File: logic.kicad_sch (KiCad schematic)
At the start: 25 parts, among them J101 PogoPin, J102 PogoPin, Q101 NMOS, U101 ATtiny404-SS

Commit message: led
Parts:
- removed D102, D104, D107, D108: LED, LED_SMD:LED_PLCC_2835_Handsoldering, symbol Device:LED
- removed R104, R107, R108: 47Ω, Resistor_SMD:R_1206_3216Metric_Pad1.30x1.75mm_HandSolder, symbol Device:R
- added D101: LED, LED_SMD:LED_PLCC_2835_Handsoldering, symbol Device:LED
- added J101: PogoPin, LIB:0906015207614110, symbol Connector:Conn_01x01_Pin
- added Q101: NMOS, Package_TO_SOT_SMD:SOT-23-3, symbol Simulation_SPICE:NMOS
- added R101: 47Ω, Resistor_SMD:R_1206_3216Metric_Pad1.30x1.75mm_HandSolder, symbol Device:R
- added R103: 100Ω, Resistor_SMD:R_1206_3216Metric_Pad1.30x1.75mm_HandSolder, symbol Device:R
- R102: value 47Ω -> 10kΩ; manf# ERJ-P08J470V -> ERJ-8GEYJ103V
- renumbered D101 to D102, D106 to D104, D109 to D105, D110 to D106, D105 to D107, J101 to J102, J102 to J103, Q101 to Q102, R101 to R104, R106 to R105, R109 to R106, R103 to R107, R105 to R108, R110 to R109, R111 to R110
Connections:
- net +5V: now also R101.2; no longer R102.2
- net GND: now also R102.2, Q101.3 (S)
- net at R102.1: now also Q101.2 (G), R103.1
- new net: D101.2 (A), R101.1
- new net: D101.1 (K), Q101.1 (D)
- new net *_LED: R103.2
- new net *_S: J101.1 (Pin_1)

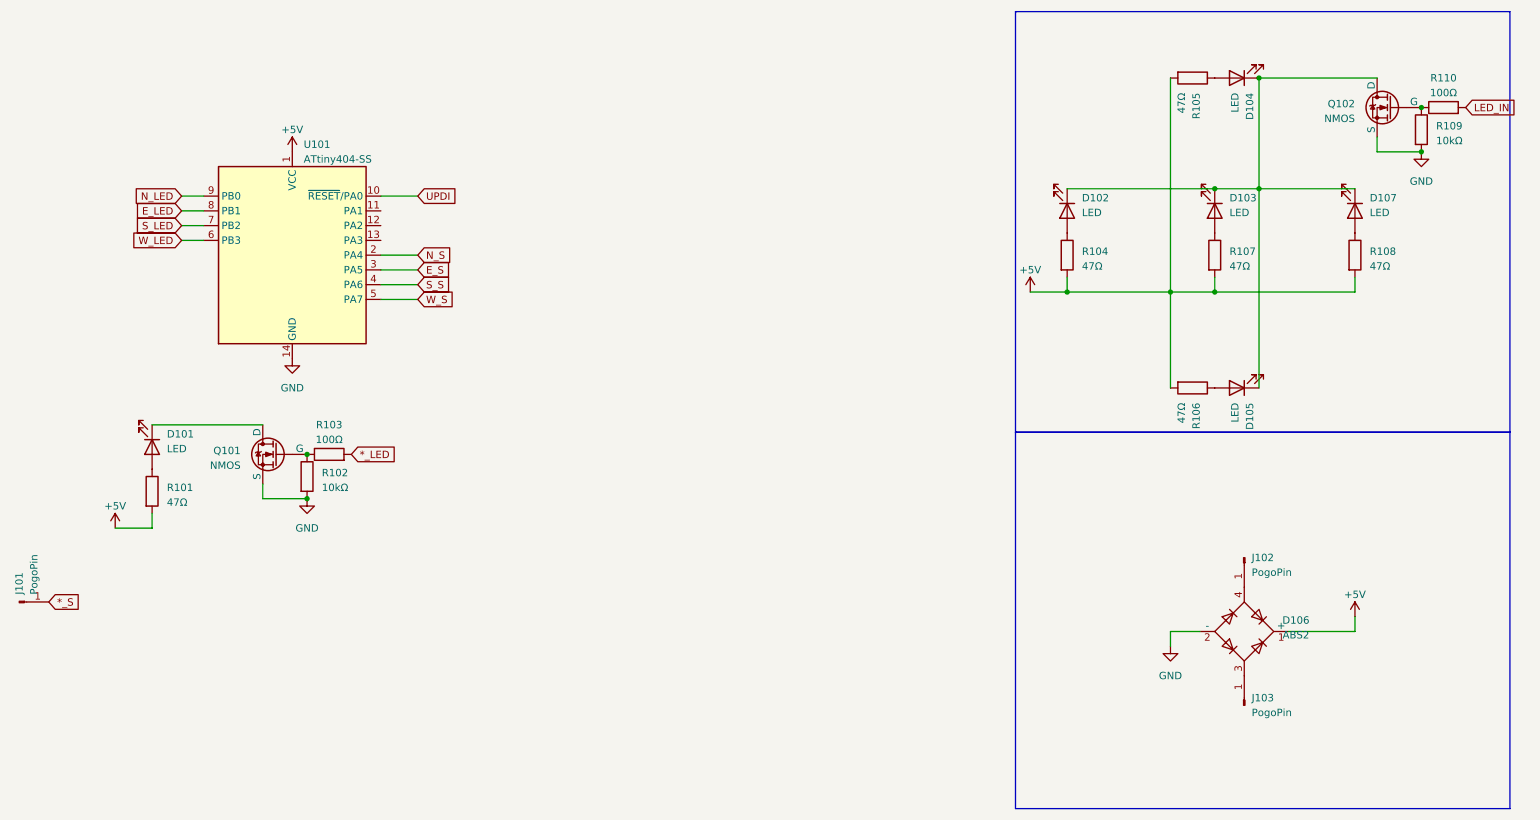
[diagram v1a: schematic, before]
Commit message: block&led
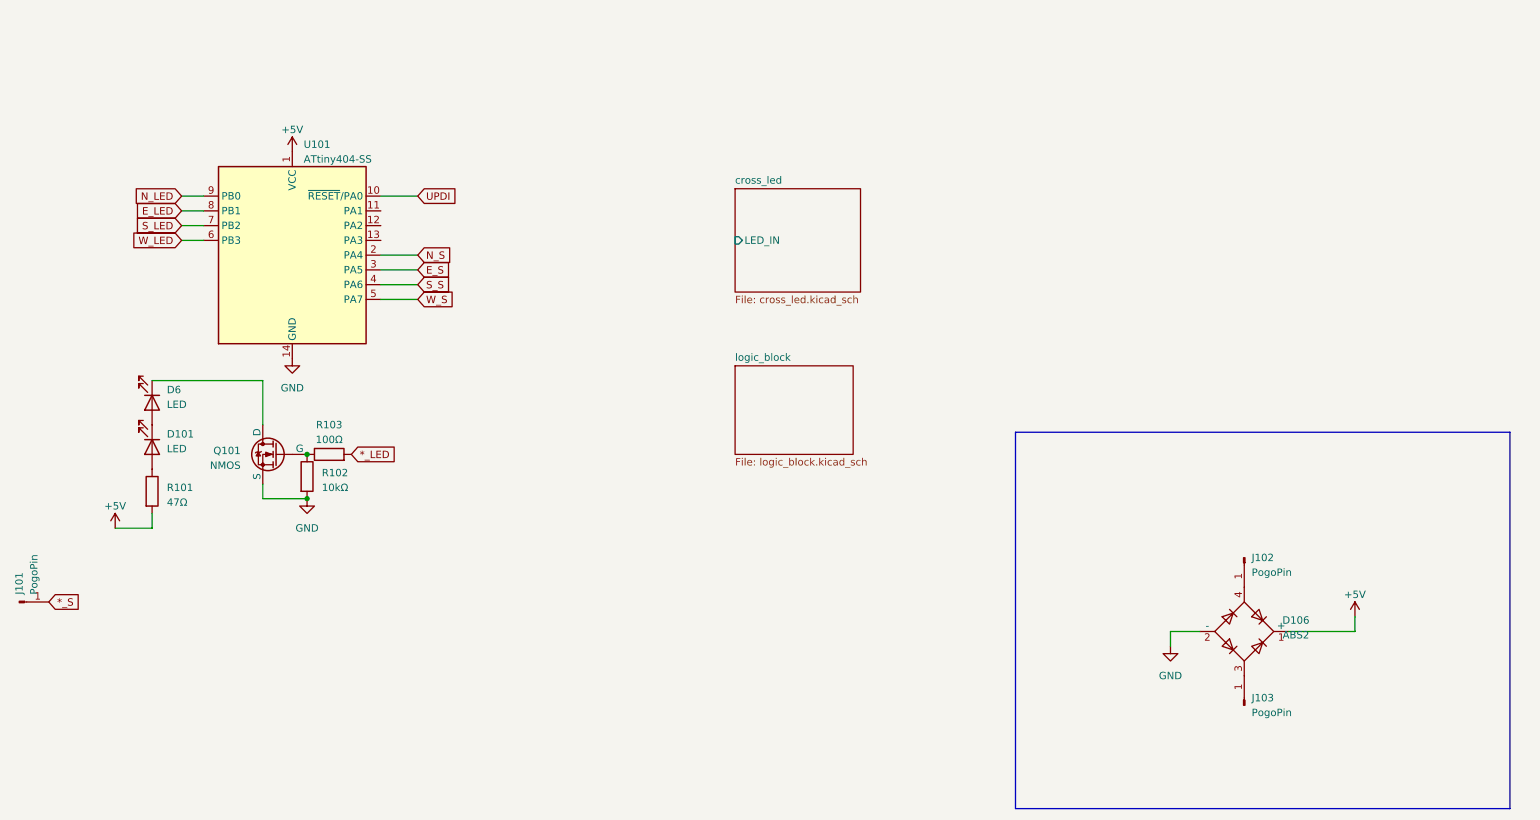
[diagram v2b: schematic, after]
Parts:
- removed D102, D103, D104, D105, D107: LED, LED_SMD:LED_PLCC_2835_Handsoldering, symbol Device:LED
- removed Q102: NMOS, Package_TO_SOT_SMD:SOT-23-3, symbol Simulation_SPICE:NMOS
- removed R104, R105, R106, R107, R108: 47Ω, Resistor_SMD:R_1206_3216Metric_Pad1.30x1.75mm_HandSolder, symbol Device:R
- removed R109: 10kΩ, Resistor_SMD:R_1206_3216Metric_Pad1.30x1.75mm_HandSolder, symbol Device:R
- removed R110: 100Ω, Resistor_SMD:R_1206_3216Metric_Pad1.30x1.75mm_HandSolder, symbol Device:R
- added D6: LED, LED_SMD:LED_PLCC_2835_Handsoldering, symbol Device:LED
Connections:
- net at D101.1 (K): now also D6.2 (A); no longer Q101.1 (D)
- new net: D6.1 (K), Q101.1 (D)
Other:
- added sheet cross_led (cross_led.kicad_sch)
- added sheet logic_block (logic_block.kicad_sch)

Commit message: all
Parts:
- removed D101, D6: LED, LED_SMD:LED_PLCC_2835_Handsoldering, symbol Device:LED
- removed J101: PogoPin, LIB:0906015207614110, symbol Connector:Conn_01x01_Pin
- removed Q101: NMOS, Package_TO_SOT_SMD:SOT-23-3, symbol Simulation_SPICE:NMOS
- removed R101: 47Ω, Resistor_SMD:R_1206_3216Metric_Pad1.30x1.75mm_HandSolder, symbol Device:R
- removed R102: 10kΩ, Resistor_SMD:R_1206_3216Metric_Pad1.30x1.75mm_HandSolder, symbol Device:R
- removed R103: 100Ω, Resistor_SMD:R_1206_3216Metric_Pad1.30x1.75mm_HandSolder, symbol Device:R
- removed U101: ATtiny404-SS, Package_SO:SOIC-14_3.9x8.7mm_P1.27mm, symbol MCU_Microchip_ATtiny:ATtiny404-SS
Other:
- added sheet block_socket (block_socket.kicad_sch)
